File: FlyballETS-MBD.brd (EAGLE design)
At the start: 53.3 x 55.9 mm, 17 parts, among them Q1 BC557, Q2 BC557

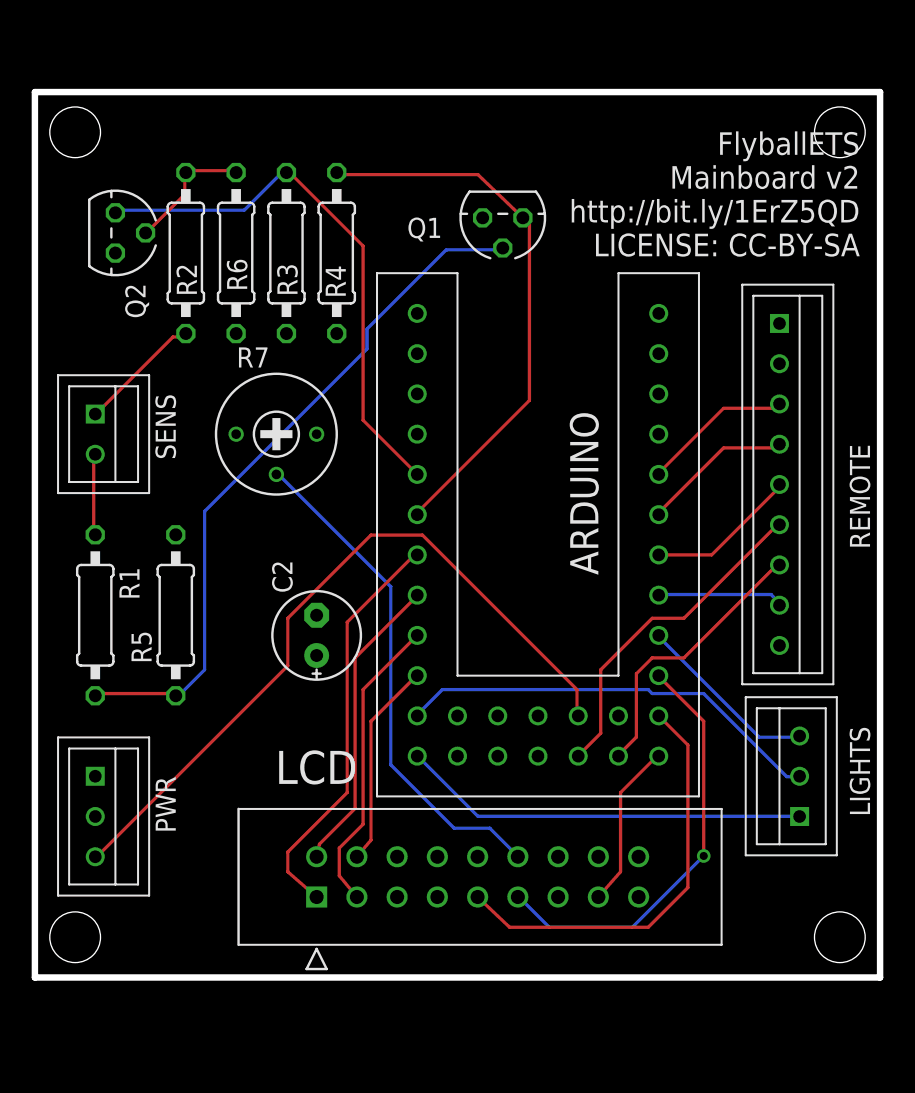
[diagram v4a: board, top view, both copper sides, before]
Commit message: Fixed JST XH pin numbering
Updated bt_con-jst-xh.lbr library with swapped pin numbering.
Updated all board designs with updated library so they have the
connectors the right way around
Fixes #4
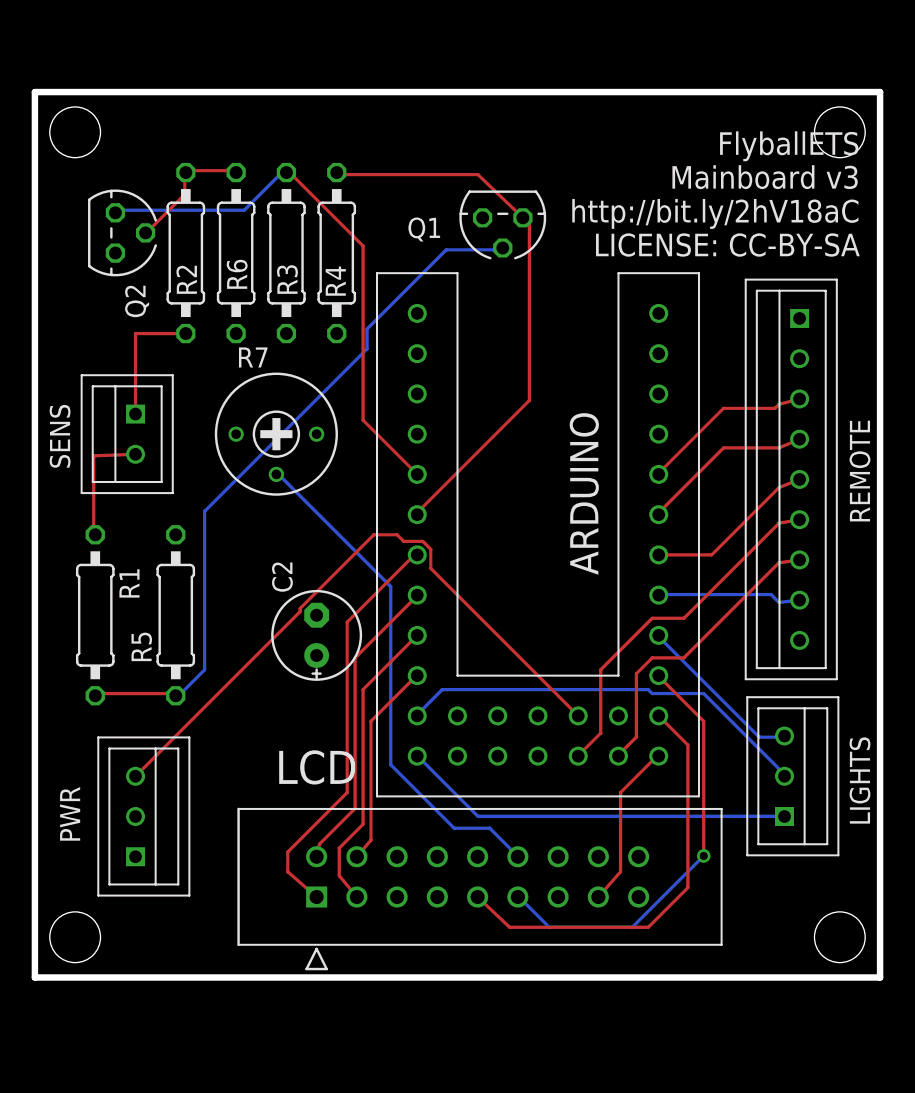
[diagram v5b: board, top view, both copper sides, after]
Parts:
- REMOTE: value 09-JST -> 09-JST-B9B-XH-A
- moved PWR 2.54 mm to (8.89, 15.2)
- moved SENS 2.54 mm to (8.89, 38.1), turned to 90 degrees
- moved REMOTE 1.31 mm to (50.8, 37.8), turned to 90 degrees
- moved LIGHTS 0.95 mm to (49.8, 17.8), turned to 270 degrees
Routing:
- net VSENS: track 46.3 -> 39.8 mm
- net N$1: track 5.14 -> 7.64 mm
- net D0: track 9.49 -> 10.8 mm
- net D3: track 21.2 -> 22.4 mm
- net D2: track 9.55 -> 10.7 mm
- net D1: track 9.62 -> 10.8 mm
- net D4: track 17.7 -> 18.9 mm
- net D5: track 7.98 -> 9.11 mm
- net RCLK: track 11.6 -> 10.6 mm
- net DATA: track 25.7 -> 24.7 mm
- net CLK: track 27.1 -> 26.4 mm
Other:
- board text added: "FlyballETS Mainboard v3 http://bit.ly/2hV18aC LICENSE: CC-BY-SA"
- board text removed: "FlyballETS Mainboard v2 http://bit.ly/1ErZ5QD LICENSE: CC-BY-SA"
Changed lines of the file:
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@@
 <?xml version="1.0" encoding="utf-8"?>
 <!DOCTYPE eagle SYSTEM "eagle.dtd">
-<eagle version="7.5.0">
+<eagle version="8.2.2">
 <drawing>
 <settings>
@@
 <text x="38.1" y="30.48" size="1.778" layer="21" rot="R90">ARDUINO</text>
 <text x="54.61" y="58.42" size="1.4224" layer="21" rot="R180">FlyballETS
-Mainboard v2
-http://bit.ly/1ErZ5QD
+Mainboard v3
+http://bit.ly/2hV18aC
 LICENSE: CC-BY-SA</text>
 <text x="22.86" y="-30.48" size="2.54" layer="48">FlyballETS
-Mainboard v2
-http://bit.ly/1ErZ5QD
+Mainboard v3
+http://bit.ly/2hV18aC
 LICENSE: CC-BY-SA</text>
 <text x="74.93" y="-17.78" size="2.54" layer="48">Alex Goris</text>
@@
 <attribute name="NAME" x="17.7038" y="17.2974" size="2.0828" layer="25" ratio="10" rot="SR0"/>
 </element>
-<element name="LIGHTS" library="bt_con-jst-xh" package="B3B-XH" value="03-JST-B3B-XH-A" x="50.8" y="17.78" smashed="yes" rot="R90">
-<attribute name="NAME" x="55.245" y="15.24" size="1.27" layer="21" rot="R90"/>
-</element>
-<element name="PWR" library="bt_con-jst-xh" package="B3B-XH" value="03-JST-B3B-XH-A" x="6.35" y="15.24" smashed="yes" rot="R270">
-<attribute name="NAME" x="10.16" y="17.78" size="1.27" layer="21" rot="R270"/>
-</element>
-<element name="SENS" library="bt_con-jst-xh" package="B2B-XH" value="02-JST" x="6.35" y="38.1" smashed="yes" rot="R270">
-<attribute name="NAME" x="10.16" y="41.91" size="1.27" layer="21" rot="R270"/>
-</element>
-<element name="REMOTE" library="bt_con-jst-xh" package="B9B-XH" value="09-JST" x="49.53" y="37.465" smashed="yes" rot="R270">
-<attribute name="NAME" x="53.975" y="38.735" size="1.27" layer="21" rot="R270"/>
+<element name="LIGHTS" library="bt_con-jst-xh" package="B3B-XH" value="03-JST-B3B-XH-A" x="49.8475" y="17.78" smashed="yes" rot="R270">
+<attribute name="NAME" x="53.975" y="20.32" size="1.27" layer="21" rot="R270"/>
+</element>
+<element name="PWR" library="bt_con-jst-xh" package="B3B-XH" value="03-JST-B3B-XH-A" x="8.89" y="15.24" smashed="yes" rot="R270">
+<attribute name="NAME" x="4.1275" y="17.145" size="1.27" layer="21" rot="R270"/>
+</element>
+<element name="SENS" library="bt_con-jst-xh" package="B2B-XH" value="02-JST" x="8.89" y="38.1" smashed="yes" rot="R90">
+<attribute name="NAME" x="4.7625" y="37.1475" size="1.27" layer="21" rot="R90"/>
+</element>
+<element name="REMOTE" library="bt_con-jst-xh" package="B9B-XH" value="09-JST-B9B-XH-A" x="50.8" y="37.7825" smashed="yes" rot="R90">
+<attribute name="NAME" x="53.975" y="40.3225" size="1.27" layer="21" rot="R270"/>
 </element>
 </elements>
@@
 <wire x1="49.5" y1="41.25" x2="49.25" y2="41" width="0.2032" layer="1"/>
 <wire x1="42" y1="37" x2="41.91" y2="36.83" width="0.2032" layer="1"/>
-<wire x1="49.5" y1="41.25" x2="49.53" y2="41.275" width="0.2032" layer="1"/>
+<wire x1="49.5" y1="41.25" x2="50.8" y2="41.5925" width="0.2032" layer="1"/>
 </signal>
 <signal name="+5V">
@@
 <wire x1="49.5" y1="38.5" x2="46" y2="38.5" width="0.2032" layer="1"/>
 <wire x1="42" y1="34.5" x2="41.91" y2="34.29" width="0.2032" layer="1"/>
-<wire x1="49.5" y1="38.5" x2="49.53" y2="38.735" width="0.2032" layer="1"/>
+<wire x1="49.5" y1="38.5" x2="50.8" y2="39.0525" width="0.2032" layer="1"/>
 </signal>
 <signal name="D2">
@@
 <wire x1="45.25" y1="31.75" x2="41.91" y2="31.75" width="0.2032" layer="1"/>
 <wire x1="49.5" y1="36" x2="45.25" y2="31.75" width="0.2032" layer="1"/>
-<wire x1="49.5" y1="36" x2="49.53" y2="36.195" width="0.2032" layer="1"/>
+<wire x1="49.5" y1="36" x2="50.8" y2="36.5125" width="0.2032" layer="1"/>
 </signal>
 <signal name="D3">
@@
 <wire x1="49.5" y1="33.75" x2="43.5" y2="27.75" width="0.2032" layer="1"/>
 <wire x1="37" y1="19.25" x2="36.83" y2="19.05" width="0.2032" layer="1"/>
-<wire x1="49.5" y1="33.75" x2="49.53" y2="33.655" width="0.2032" layer="1"/>
+<wire x1="49.5" y1="33.75" x2="50.8" y2="33.9725" width="0.2032" layer="1"/>
 </signal>
 <signal name="D4">
@@
 <wire x1="49.5" y1="31.25" x2="43.5" y2="25.25" width="0.2032" layer="1"/>
 <wire x1="39.5" y1="19.25" x2="39.37" y2="19.05" width="0.2032" layer="1"/>
-<wire x1="49.5" y1="31.25" x2="49.53" y2="31.115" width="0.2032" layer="1"/>
+<wire x1="49.5" y1="31.25" x2="50.8" y2="31.4325" width="0.2032" layer="1"/>
 </signal>
 <signal name="D5">
@@
 <wire x1="49.5" y1="28.75" x2="49" y2="29.25" width="0.2032" layer="16"/>
 <wire x1="42" y1="29.25" x2="41.91" y2="29.21" width="0.2032" layer="16"/>
-<wire x1="49.5" y1="28.75" x2="49.53" y2="28.575" width="0.2032" layer="16"/>
+<wire x1="49.5" y1="28.75" x2="50.8" y2="28.8925" width="0.2032" layer="16"/>
 </signal>
 <signal name="E1">
@@
 <contactref element="LIGHTS" pad="P$1"/>
 <wire x1="30.5" y1="15.25" x2="26.75" y2="19" width="0.2032" layer="16"/>
-<wire x1="50.75" y1="15.25" x2="30.5" y2="15.25" width="0.2032" layer="16"/>
+<wire x1="49.7975" y1="15.25" x2="30.5" y2="15.25" width="0.2032" layer="16"/>
 <wire x1="26.75" y1="19" x2="26.67" y2="19.05" width="0.2032" layer="16"/>
-<wire x1="50.75" y1="15.25" x2="50.8" y2="15.24" width="0.2032" layer="16"/>
+<wire x1="49.7975" y1="15.25" x2="49.8475" y2="15.24" width="0" layer="19" extent="16-16"/>
 </signal>
 <signal name="CLK">
@@
 <wire x1="44.75" y1="23" x2="41.5" y2="23" width="0.2032" layer="16"/>
 <wire x1="50" y1="17.75" x2="44.75" y2="23" width="0.2032" layer="16"/>
-<wire x1="50.75" y1="17.75" x2="50" y2="17.75" width="0.2032" layer="16"/>
 <wire x1="26.75" y1="21.75" x2="26.67" y2="21.59" width="0.2032" layer="16"/>
-<wire x1="50.75" y1="17.75" x2="50.8" y2="17.78" width="0.2032" layer="16"/>
+<wire x1="49.7975" y1="17.75" x2="49.8475" y2="17.78" width="0.2032" layer="16"/>
+<wire x1="50" y1="17.75" x2="49.8475" y2="17.78" width="0" layer="19" extent="16-16"/>
 </signal>
 <signal name="RCLK">
@@
 <contactref element="LIGHTS" pad="P$3"/>
 <wire x1="48.25" y1="20.25" x2="42" y2="26.5" width="0.2032" layer="16"/>
-<wire x1="50.75" y1="20.25" x2="48.25" y2="20.25" width="0.2032" layer="16"/>
+<wire x1="49.7975" y1="20.25" x2="48.25" y2="20.25" width="0.2032" layer="16"/>
 <wire x1="42" y1="26.5" x2="41.91" y2="26.67" width="0.2032" layer="16"/>
-<wire x1="50.75" y1="20.25" x2="50.8" y2="20.32" width="0.2032" layer="16"/>
+<wire x1="49.7975" y1="20.25" x2="49.8475" y2="20.32" width="0" layer="19" extent="16-16"/>
 </signal>
 <signal name="N$3">
@@
 <contactref element="ARDUINO" pad="A6"/>
 <contactref element="PWR" pad="P$3"/>
-<wire x1="18.5" y1="24.75" x2="6.5" y2="12.75" width="0.2032" layer="1"/>
-<wire x1="18.5" y1="27.75" x2="18.5" y2="24.75" width="0.2032" layer="1"/>
-<wire x1="23.75" y1="33" x2="18.5" y2="27.75" width="0.2032" layer="1"/>
-<wire x1="27" y1="33" x2="23.75" y2="33" width="0.2032" layer="1"/>
-<wire x1="36.75" y1="23.25" x2="27" y2="33" width="0.2032" layer="1"/>
-<wire x1="36.75" y1="21.75" x2="36.75" y2="23.25" width="0.2032" layer="1"/>
-<wire x1="6.5" y1="12.75" x2="6.35" y2="12.7" width="0.2032" layer="1"/>
-<wire x1="36.75" y1="21.75" x2="36.83" y2="21.59" width="0.2032" layer="1"/>
+<wire x1="8.89" y1="17.78" x2="19.2786" y2="28.1686" width="0.2032" layer="1"/>
+<wire x1="19.2786" y1="28.1686" x2="19.2786" y2="28.3713625" width="0.2032" layer="1"/>
+<wire x1="19.2786" y1="28.3713625" x2="23.9272375" y2="33.02" width="0.2032" layer="1"/>
+<wire x1="23.9272375" y1="33.02" x2="25.4" y2="33.02" width="0.2032" layer="1"/>
+<wire x1="27.02374375" y1="32.604" x2="27.524" y2="32.10374375" width="0.2032" layer="1"/>
+<wire x1="25.4" y1="33.02" x2="25.816" y2="32.604" width="0.2032" layer="1"/>
+<wire x1="27.524" y1="30.896" x2="36.83" y2="21.59" width="0.2032" layer="1"/>
+<wire x1="25.816" y1="32.604" x2="27.02374375" y2="32.604" width="0.2032" layer="1"/>
+<wire x1="27.524" y1="32.10374375" x2="27.524" y2="30.896" width="0.2032" layer="1"/>
 </signal>
 <signal name="N$1">
@@
 <contactref element="SENS" pad="P$2"/>
 <wire x1="6.25" y1="33.25" x2="6.25" y2="38" width="0.2032" layer="1"/>
-<wire x1="6.25" y1="38" x2="6.35" y2="38.1" width="0.2032" layer="1"/>
+<wire x1="6.25" y1="38" x2="8.89" y2="38.1" width="0.2032" layer="1"/>
 <wire x1="6.25" y1="33.25" x2="6.35" y2="33.02" width="0.2032" layer="1"/>
 </signal>
@@
 <contactref element="R2" pad="1"/>
 <contactref element="SENS" pad="P$1"/>
-<wire x1="11.25" y1="45.5" x2="6.5" y2="40.75" width="0.2032" layer="1"/>
-<wire x1="12" y1="45.5" x2="11.25" y2="45.5" width="0.2032" layer="1"/>
-<wire x1="6.5" y1="40.75" x2="6.35" y2="40.64" width="0.2032" layer="1"/>
-<wire x1="12" y1="45.5" x2="12.065" y2="45.72" width="0.2032" layer="1"/>
+<wire x1="8.89" y1="40.64" x2="8.89" y2="45.72" width="0.2032" layer="1"/>
+<wire x1="8.89" y1="45.72" x2="12.065" y2="45.72" width="0.2032" layer="1"/>
 </signal>
 </signals>
